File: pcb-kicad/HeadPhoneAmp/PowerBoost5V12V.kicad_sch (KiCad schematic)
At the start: 39 parts, among them Q1 Q_PNP_ECB_BRT, U1 VREG_TPS6103X, U2 MCP73871

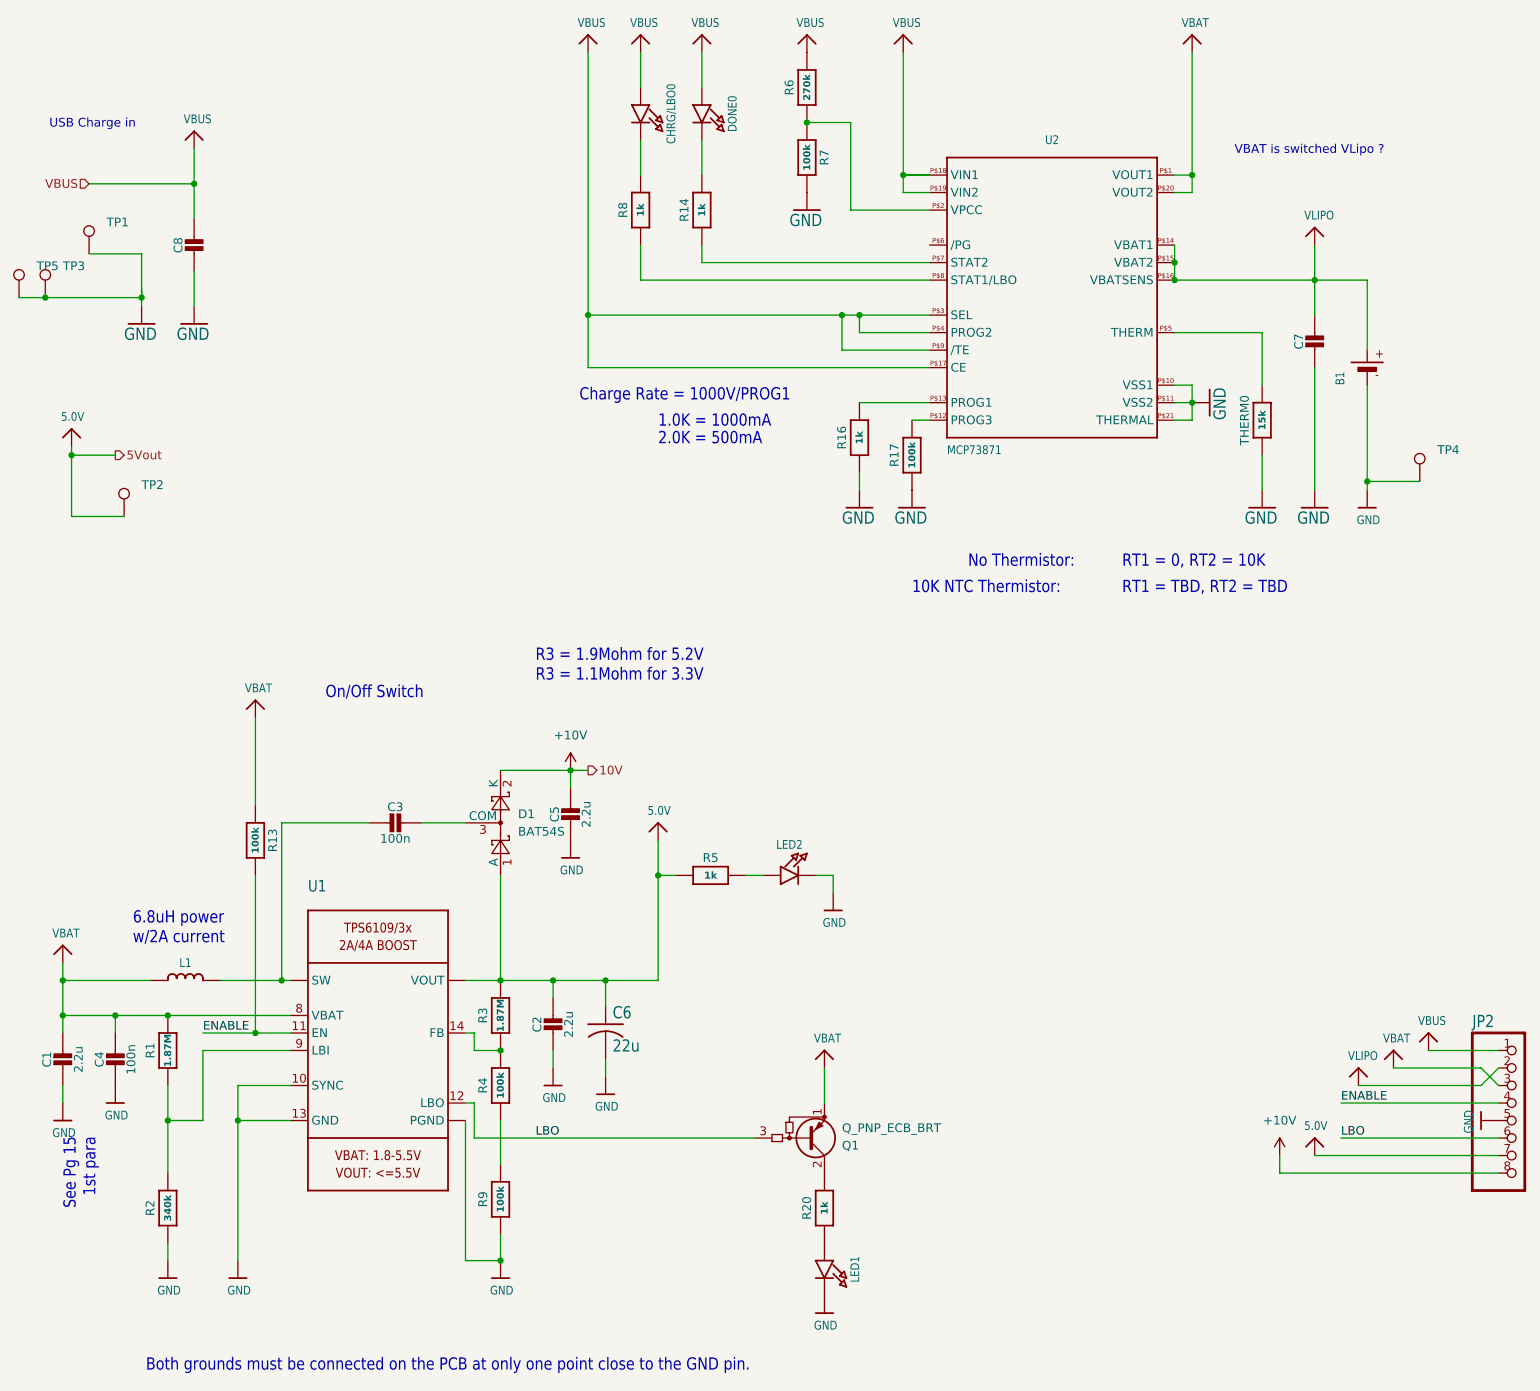
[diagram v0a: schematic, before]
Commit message: Fixed PowerBlock PCB it's v0.2 now
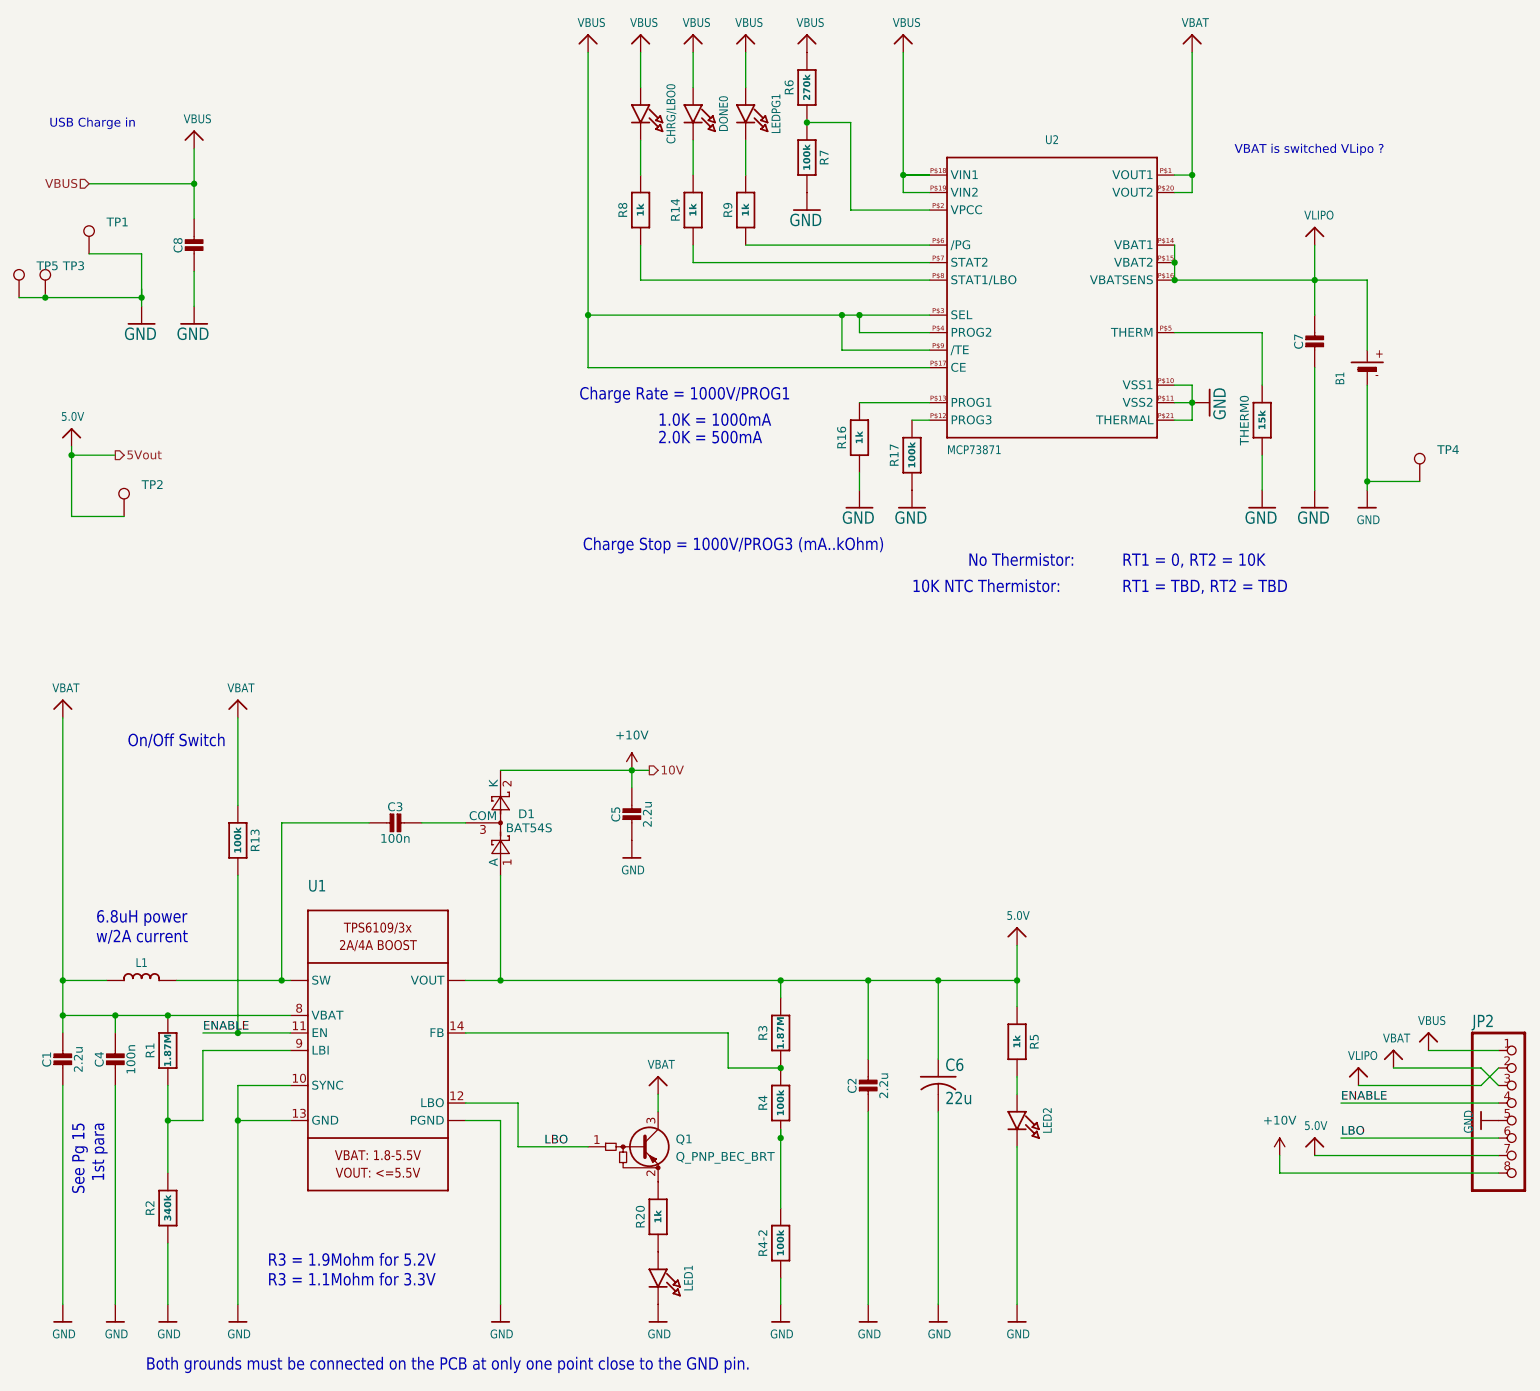
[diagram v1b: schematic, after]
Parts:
- removed Q1: Q_PNP_ECB_BRT, Package_TO_SOT_SMD:SOT-23, symbol Device:Q_PNP_ECB_BRT
- added LEDPG1: PG, Adafruit PowerBoost 1000C Rev B:CHIPLED_0805_NOOUTLINE, symbol Adafruit PowerBoost 1000C Rev B-eagle-import:LED0805_NOOUTLINE
- added Q1: Q_PNP_BEC_BRT, Package_TO_SOT_SMD:SOT-23, symbol Device:Q_PNP_BEC_BRT
- added R9: 1k, Resistor_SMD:R_0603_1608Metric_Pad0.98x0.95mm_HandSolder, symbol Adafruit PowerBoost 1000C Rev B-eagle-import:RESISTOR0805_NOOUTLINE
- renumbered R9 to R4-2
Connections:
- net LBO: now also Q1.1 (B)
- net VBAT: now also Q1.3 (C)
- net VBUS: now also LEDPG1.A
- net at R20.2: now also Q1.2 (E)
- net at U2.P$6 (/PG): now also R9.1
- new net: LEDPG1.C, R9.2
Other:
- note added: "Charge Stop = 1000V/PROG3 (mA..kOhm)"
- moved on the sheet: C2, C5, C6, DONE0, L1, LED1, LED2, R13, R14, R20, R3, R4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
